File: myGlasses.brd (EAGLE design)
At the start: 39.2 x 17.3 mm, 16 parts

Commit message: Lunettes petit format corrige
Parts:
- moved R5 11.7 mm to (8.29, 13.6)
- moved BATT 10.8 mm to (2.19, 11.6)
- moved C2 10.2 mm to (1.98, 7.69)
- moved LED1 8.57 mm to (11.0, 12.7), flipped to the bottom
- moved USB 7.54 mm to (5.51, 1.64), turned to 0 degrees
- moved LDO3.3 7.46 mm to (13.3, 6.79), flipped to the bottom, turned to 0 degrees
- moved R3 7.37 mm to (30.8, 6.92)
- moved TRI_LED 6.39 mm to (30.1, 7.73), flipped to the bottom, turned to 90 degrees
- moved SWD 5.48 mm to (30.8, 1.86)
- moved CHARG 5.36 mm to (5.49, 3.56), flipped to the bottom, turned to 270 degrees
- moved N550 4.56 mm to (25.0, 8.96)
- moved R2 4.53 mm to (28.2, 6.97)
- moved C1 4.03 mm to (5.59, 9.39)
- moved INTER 3.76 mm to (20.3, 12.7)
- moved R4 2.96 mm to (9.44, 7.93), turned to 270 degrees
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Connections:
- net 3.3V: now also TRI_LED.A
- net GND: no longer TRI_LED.A
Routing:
- net GND: track 101.8 -> 57.3 mm
- net N$9: track 24.5 -> 3.14 mm, vias 0 -> 1
- net N$7: track 14.9 -> 7.26 mm, vias 0 -> 1
- net N$4: track 10.9 -> 3.62 mm, vias 0 -> 1
- net N$2: track 11.8 -> 6.37 mm, vias 0 -> 1
- net N$5: track 15.1 -> 19.9 mm, vias 3 -> 1
- net N$8: track 5.31 -> 9.85 mm, vias 0 -> 1
- net 3.3V: track 14.2 -> 17.0 mm
- net N$1: track 38.2 -> 40.4 mm
- net VCC-ISO: track 17.0 -> 18.5 mm, vias 1 -> 0
- net N$12: track 9.62 -> 8.24 mm
- net N$10: track 12.4 -> 11.2 mm
- net N$11: track 6.46 -> 7.62 mm
- net N$6: track 10.5 -> 9.75 mm
- net N$3: track 5.40 -> 5.05 mm, vias 0 -> 1
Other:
- board size 39.2 x 17.3 mm -> 33.2 x 15.3 mm

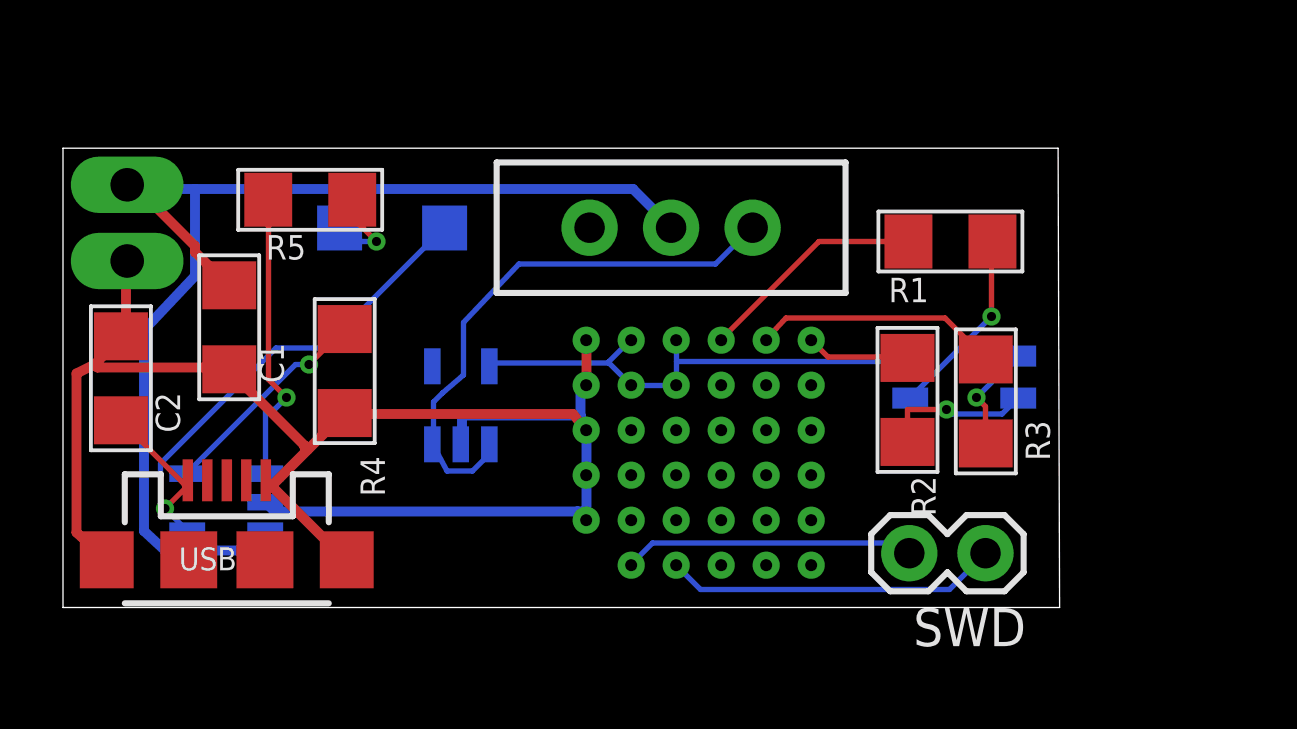
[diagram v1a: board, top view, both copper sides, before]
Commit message: Put a ML1220 cell First routing
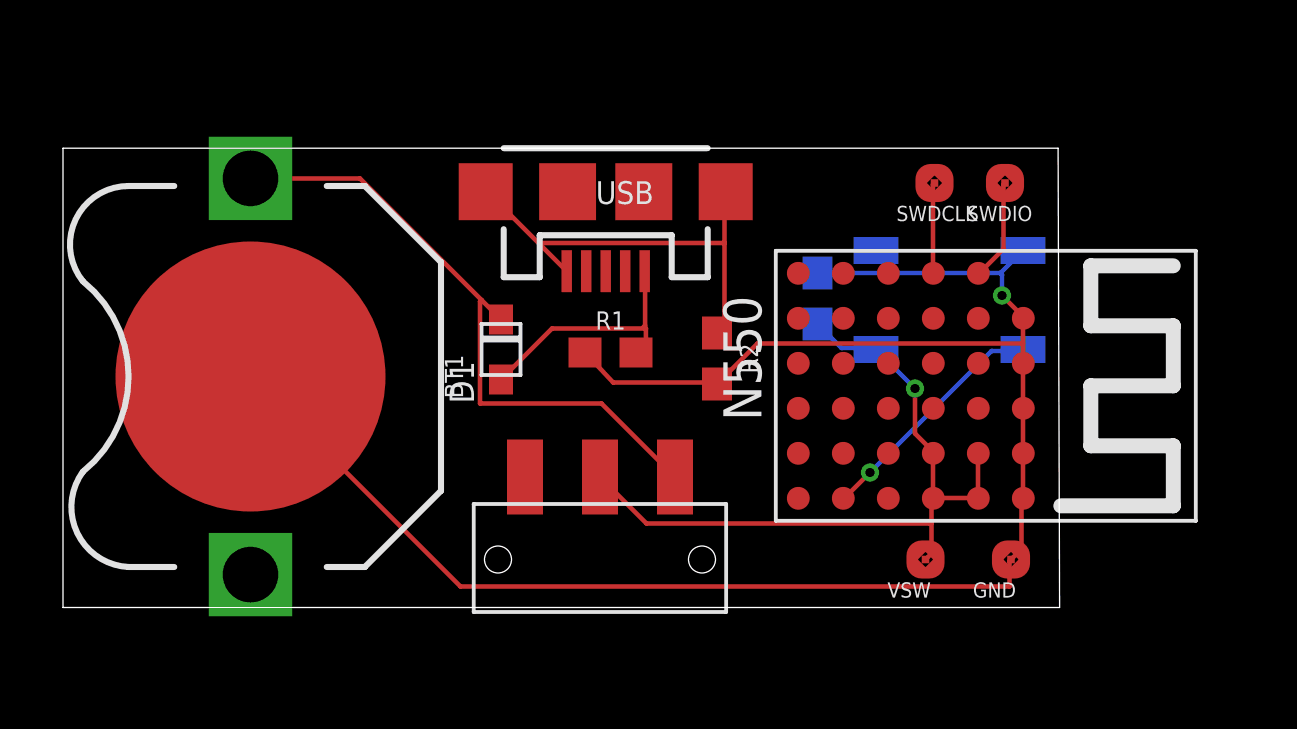
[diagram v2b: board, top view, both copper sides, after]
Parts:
- removed BATT: (no value), SparkFun-Connectors:1X02_LONGPADS
- removed C2: 4.7uF, microbuilder:1206
- removed CHARG: MCP73831/OT, adafruit:SOT23-5L
- removed INTER: (no value), SparkFun-Electromechanical:SWITCH-SPDT_LOCK.007S
- removed LDO3.3: V_REG_LDOSMD, SparkFun-PowerIC:SOT23-5
- removed LED1: (no value), adafruit:CHIPLED_1206
- removed R3: 220, microbuilder:1206
- removed R4: 2k, microbuilder:1206
- removed R5: 330, microbuilder:1206
- removed SWD: (no value), SparkFun-Connectors:1X02
- removed TRI_LED: LED-TRICOLOR, SparkFun-LED:LED-TRICOLOR-SMD
- added BT1: (no value), SparkFun-Batteries:BATTCON_12MM_PTH
- added D1: DB2J314, adafruit:SOD-323F
- added GND, SWDCLK, SWDIO, VSW: TESTPOINT, test_points:TESTPOINT
- added L1: WS2812B, adafruit:WS2812B
- added U$1: JS102011SAQN, JS102011SAQN:JS102011SAQN
- C1: device microbuilder:1206 -> SparkFun-Capacitors:0603
- N550: value N548 -> N5150; device N548:N548 -> N5:N5150
- R1: value 220 -> 1.2k; device microbuilder:1206 -> SparkFun-Resistors:0603
- R2: value 220 -> 680; device microbuilder:1206 -> SparkFun-Resistors:0603
- moved C1 19.6 mm to (25.2, 10.3), flipped to the bottom
- moved USB 17.6 mm to (18.1, 13.9), turned to 180 degrees
- moved R1 11.9 mm to (18.3, 8.55)
- moved N550 7.41 mm to (32.1, 11.2), turned to 90 degrees
- moved R2 6.50 mm to (21.9, 8.35)
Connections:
- removed net N$10: N550.SWDCLK, SWD.1
- removed net N$11: N550.P024, R1.1
- removed net N$12: N550.P030, R3.1
- removed net N$13: N550.P031, R2.1
- removed net N$2: R1.2, TRI_LED.R
- removed net N$4: R3.2, TRI_LED.B
- removed net N$5: C2.1, CHARG.4, LED1.A, USB.VBUS
- removed net N$6: N550.SWDIO, SWD.2
- removed net N$7: CHARG.5, R4.1
- removed net N$8: CHARG.1, R5.2
- removed net N$9: LED1.C, R5.1
- removed net VCC-ISO: INTER.1, LDO3.3.1, LDO3.3.3
- new net BATP: BT1.VCC@1, D1.C, U$1.P$3
- new net NEO: L1.4-DIN, N550.E6
- new net VSW: C1.1, L1.1-VDD, N550.B5, N550.B6, N550.C5, N550.C6, U$1.P$2, VSW.P$1
- new net VUSB: D1.A, R1.2, USB.VBUS
- net 3.3V: now also R2.1, USB.GND, USB.MT1, USB.MT2; no longer LDO3.3.5, N550.B5, N550.B6, N550.C5, N550.C6, TRI_LED.A
- net GND: now also BT1.GND, C1.2, GND.P$1, L1.3-GND, R1.1, R2.2; no longer BATT.1, C1.1, C2.2, CHARG.2, LDO3.3.2, R4.2, USB.GND, USB.MT1, USB.MT2
- net N$1: now also N550.B1, SWDIO.P$1; no longer BATT.2, C1.2, CHARG.3, INTER.2
- net N$3: now also N550.C1, SWDCLK.P$1; no longer R2.2, TRI_LED.G
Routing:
- net N$1: track 40.4 -> 3.39 mm
- net VSW: track 0.00 -> 24.9 mm, vias 0 -> 1
- net BATP: track 0.00 -> 21.3 mm
- net N$5: track 19.9 -> 0.00 mm, vias 1 -> 0
- net VCC-ISO: track 18.5 -> 0.00 mm
- net N$10: track 11.2 -> 0.00 mm
- net N$8: track 9.85 -> 0.00 mm, vias 1 -> 0
- net N$6: track 9.75 -> 0.00 mm
- net VUSB: track 0.00 -> 8.63 mm
- net N$12: track 8.24 -> 0.00 mm
- net NEO: track 0.00 -> 8.04 mm, vias 0 -> 1
- net N$11: track 7.62 -> 0.00 mm
- net N$7: track 7.26 -> 0.00 mm, vias 1 -> 0
- net N$2: track 6.37 -> 0.00 mm, vias 1 -> 0
- net GND: track 57.3 -> 61.9 mm, vias 0 -> 1
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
